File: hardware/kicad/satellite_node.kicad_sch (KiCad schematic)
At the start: 4 parts, among them U1 Seeed Studio XIAO ESP32S3, U2 SmartElex KX134-1211 (acceler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, U3 INMP441 (I2S microphone), U4 WS2812B x8 status ring

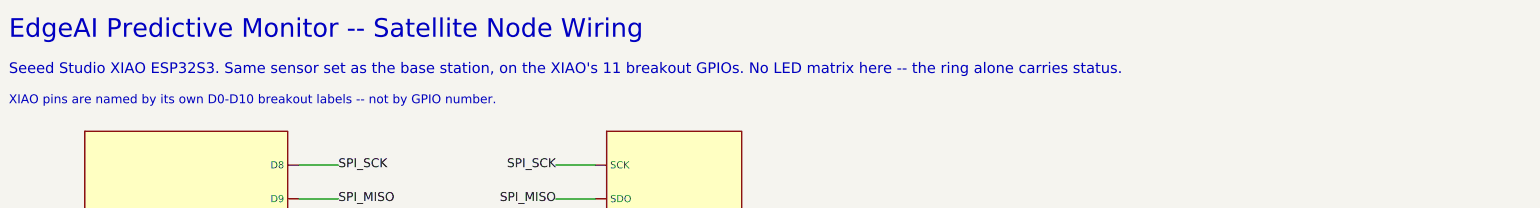
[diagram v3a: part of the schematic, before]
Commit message: schematics: shorten satellite-node subtitle to cut crop-driven whitespace
That subtitle line was the widest thing on the sheet -- 149 chars vs.
~83-134 on the other two diagrams -- so the auto-crop bounding box
stretched ~100mm past the actual circuit just to fit it, leaving a
dead strip on the right. Trimmed it to the same info in fewer words.

Co-Authored-By: Claude Sonnet 5 <noreply@anthropic.com>
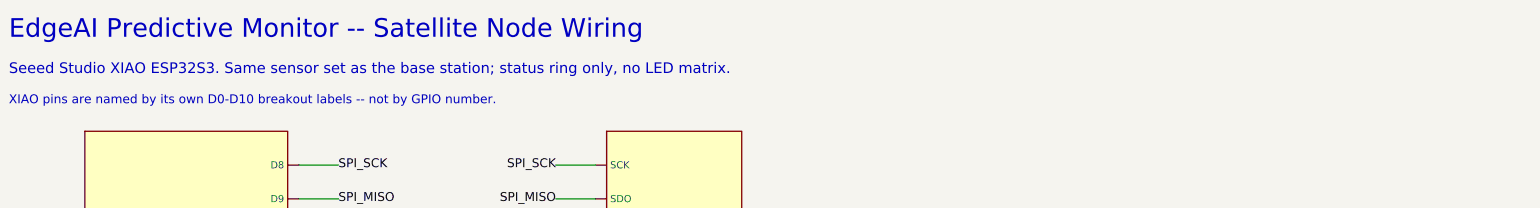
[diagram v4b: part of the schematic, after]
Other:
- note added: "Seeed Studio XIAO ESP32S3. Same sensor set as the base station; status ring only, no LED matrix."
- note removed: "Seeed Studio XIAO ESP32S3. Same sensor set as the base station, on the XIAO's 11 breakout GPIOs. No LED matrix here -- the ring alone carries status."
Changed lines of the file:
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@@
 		(effects (font (size 4.2 4.2)) (justify left))
 	)
-	(text "Seeed Studio XIAO ESP32S3. Same sensor set as the base station, on the XIAO's 11 breakout GPIOs. No LED matrix here -- the ring alone carries status."
+	(text "Seeed Studio XIAO ESP32S3. Same sensor set as the base station; status ring only, no LED matrix."
 		(exclude_from_sim no)
 		(at 20 34 0)
@@
 		(instances
 			(project "epm"
-				(path "/b0fb9a1d-4179-43c2-8546-24e0d59c6c4d"
+				(path "/f496122b-d5f3-4e05-9a34-a035c40fc367"
 					(reference "U1")
 					(unit 1)
@@
 		(on_board yes)
 		(dnp no)
-		(property "Reference" "#PWRb905"
+		(property "Reference" "#PWR1534"
 			(at 94.29 118.2 0)
 			(effects (font (size 1.27 1.27)) (hide yes))
@@
 		(instances
 			(project "epm"
-				(path "/b0fb9a1d-4179-43c2-8546-24e0d59c6c4d"
-					(reference "#PWRb905")
+				(path "/f496122b-d5f3-4e05-9a34-a035c40fc367"
+					(reference "#PWR1534")
 					(unit 1)
 				)
@@
 		(on_board yes)
 		(dnp no)
-		(property "Reference" "#PWR753b"
+		(property "Reference" "#PWR40eb"
 			(at 94.29 125.82 0)
 			(effects (font (size 1.27 1.27)) (hide yes))
@@
 		(instances
 			(project "epm"
-				(path "/b0fb9a1d-4179-43c2-8546-24e0d59c6c4d"
-					(reference "#PWR753b")
+				(path "/f496122b-d5f3-4e05-9a34-a035c40fc367"
+					(reference "#PWR40eb")
 					(unit 1)
 				)
@@
 		(on_board yes)
 		(dnp no)
-		(property "Reference" "#PWRd3a9"
+		(property "Reference" "#PWR83cc"
 			(at 94.29 133.44 0)
 			(effects (font (size 1.27 1.27)) (hide yes))
@@
 		(instances
 			(project "epm"
-				(path "/b0fb9a1d-4179-43c2-8546-24e0d59c6c4d"
-					(reference "#PWRd3a9")
+				(path "/f496122b-d5f3-4e05-9a34-a035c40fc367"
+					(reference "#PWR83cc")
 					(unit 1)
 				)
@@
 		(instances
 			(project "epm"
-				(path "/b0fb9a1d-4179-43c2-8546-24e0d59c6c4d"
+				(path "/f496122b-d5f3-4e05-9a34-a035c40fc367"
 					(reference "U2")
 					(unit 1)
@@
 		(on_board yes)
 		(dnp no)
-		(property "Reference" "#PWR9c86"
+		(property "Reference" "#PWR5d82"
 			(at 143.32999999999998 87.72 0)
 			(effects (font (size 1.27 1.27)) (hide yes))
@@
 		(instances
 			(project "epm"
-				(path "/b0fb9a1d-4179-43c2-8546-24e0d59c6c4d"
-					(reference "#PWR9c86")
+				(path "/f496122b-d5f3-4e05-9a34-a035c40fc367"
+					(reference "#PWR5d82")
 					(unit 1)
 				)
@@
 		(on_board yes)
 		(dnp no)
-		(property "Reference" "#PWRb8b9"
+		(property "Reference" "#PWR1843"
 			(at 143.32999999999998 95.34 0)
 			(effects (font (size 1.27 1.27)) (hide yes))
@@
 		(instances
 			(project "epm"
-				(path "/b0fb9a1d-4179-43c2-8546-24e0d59c6c4d"
-					(reference "#PWRb8b9")
+				(path "/f496122b-d5f3-4e05-9a34-a035c40fc367"
+					(reference "#PWR1843")
 					(unit 1)
 				)
@@
 		(instances
 			(project "epm"
-				(path "/b0fb9a1d-4179-43c2-8546-24e0d59c6c4d"
+				(path "/f496122b-d5f3-4e05-9a34-a035c40fc367"
 					(reference "U3")
 					(unit 1)
@@
 		(on_board yes)
 		(dnp no)
-		(property "Reference" "#PWR7f09"
+		(property "Reference" "#PWR40e0"
 			(at 144.60000000000002 147.20000000000002 0)
 			(effects (font (size 1.27 1.27)) (hide yes))
@@
 		(instances
 			(project "epm"
-				(path "/b0fb9a1d-4179-43c2-8546-24e0d59c6c4d"
-					(reference "#PWR7f09")
+				(path "/f496122b-d5f3-4e05-9a34-a035c40fc367"
+					(reference "#PWR40e0")
 					(unit 1)
 				)
@@
 		(on_board yes)
 		(dnp no)
-		(property "Reference" "#PWR97c5"
+		(property "Reference" "#PWR623f"
 			(at 144.60000000000002 154.82000000000002 0)
 			(effects (font (size 1.27 1.27)) (hide yes))
@@
 		(instances
 			(project "epm"
-				(path "/b0fb9a1d-4179-43c2-8546-24e0d59c6c4d"
-					(reference "#PWR97c5")
+				(path "/f496122b-d5f3-4e05-9a34-a035c40fc367"
+					(reference "#PWR623f")
 					(unit 1)
 				)
@@
 		(on_board yes)
 		(dnp no)
-		(property "Reference" "#PWR6390"
+		(property "Reference" "#PWRc5e7"
 			(at 144.60000000000002 162.44000000000003 0)
 			(effects (font (size 1.27 1.27)) (hide yes))
@@
 		(instances
 			(project "epm"
-				(path "/b0fb9a1d-4179-43c2-8546-24e0d59c6c4d"
-					(reference "#PWR6390")
+				(path "/f496122b-d5f3-4e05-9a34-a035c40fc367"
+					(reference "#PWRc5e7")
 					(unit 1)
 				)
@@
 		(instances
 			(project "epm"
-				(path "/b0fb9a1d-4179-43c2-8546-24e0d59c6c4d"
+				(path "/f496122b-d5f3-4e05-9a34-a035c40fc367"
 					(reference "U4")
 					(unit 1)
@@
 		(on_board yes)
 		(dnp no)
-		(property "Reference" "#PWR42ca"
+		(property "Reference" "#PWRbdb7"
 			(at 144.60000000000002 199.06 0)
 			(effects (font (size 1.27 1.27)) (hide yes))
@@
 		(instances
 			(project "epm"
-				(path "/b0fb9a1d-4179-43c2-8546-24e0d59c6c4d"
-					(reference "#PWR42ca")
+				(path "/f496122b-d5f3-4e05-9a34-a035c40fc367"
+					(reference "#PWRbdb7")
 					(unit 1)
 				)
@@
 		(on_board yes)
 		(dnp no)
-		(property "Reference" "#PWR17d9"
+		(property "Reference" "#PWRbfdd"
 			(at 144.60000000000002 206.68 0)
 			(effects (font (size 1.27 1.27)) (hide yes))
@@
 		(instances
 			(project "epm"
-				(path "/b0fb9a1d-4179-43c2-8546-24e0d59c6c4d"
-					(reference "#PWR17d9")
-					(unit 1)
-				)
+				(path "/f496122b-d5f3-4e05-9a34-a035c40fc367"
+					(reference "#PWRbfdd")
+					(unit 1)
+				)

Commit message: schematics: fix satellite pin map, rename accel nets, hi-res exports, KiCad projects
- satellite_node: ACC_CS/ACC_INT/MIC_WS/MIC_SD were wrong vs
  satellite/include/board_pins.h (used D3/D2/D0/D4; firmware drives
  D6/D7/D2/D3). Now transcribed straight from the header.
- base + satellite: SPI_SCK/MISO/MOSI nets renamed to ACC_SCK/ACC_MISO/
  ACC_MOSI so the accelerometer bus reads consistently with ACC_CS/ACC_INT.
- exports: SVG now --exclude-drawing-sheet; raster bumped to scale=5.0
  (~3.6-3.9k px) for headroom against Hackster's imgix auto=compress;
  report PNGs flattened to true PNG-24 (no alpha) + sibling JPEGs (q92).
  Crop simplified to a plain ink bbox.
- gen.py write_pro() now emits a real minimal .kicad_pro per board
  (sheets -> sch root UUID) so each opens as a self-contained project;
  make_bundles.py zips pro+sch+pdf into dist/ for Hackster Attachments
  (dist/ git-ignored).

Co-Authored-By: Claude Sonnet 5 <noreply@anthropic.com>
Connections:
- net SPI_MISO renamed ACC_MISO
- net SPI_MOSI renamed ACC_MOSI
- net SPI_SCK renamed ACC_SCK
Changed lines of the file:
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@@
 		(stroke (width 0) (type default))
 	)
-	(label "SPI_SCK"
+	(label "ACC_SCK"
 		(at 94.29 55.62 0)
 		(effects (font (size 2.0 2.0)) (justify left))
 	)
-	(label "SPI_MISO"
+	(label "ACC_MISO"
 		(at 94.29 63.24 0)
 		(effects (font (size 2.0 2.0)) (justify left))
 	)
-	(label "SPI_MOSI"
+	(label "ACC_MOSI"
 		(at 94.29 70.86 0)
 		(effects (font (size 2.0 2.0)) (justify left))
@@
 		(effects (font (size 2.0 2.0)) (justify left))
 	)
-	(label "SPI_SCK"
+	(label "ACC_SCK"
 		(at 143.32999999999998 55.620000000000005 0)
 		(effects (font (size 2.0 2.0)) (justify right))
 	)
-	(label "SPI_MISO"
+	(label "ACC_MISO"
 		(at 143.32999999999998 63.24 0)
 		(effects (font (size 2.0 2.0)) (justify right))
 	)
-	(label "SPI_MOSI"
+	(label "ACC_MOSI"
 		(at 143.32999999999998 70.86 0)
 		(effects (font (size 2.0 2.0)) (justify right))
@@
 		(instances
 			(project "epm"
-				(path "/f496122b-d5f3-4e05-9a34-a035c40fc367"
+				(path "/eb09b952-6273-4b00-b988-117cd571ae26"
 					(reference "U1")
 					(unit 1)
@@
 		(on_board yes)
 		(dnp no)
-		(property "Reference" "#PWR1534"
+		(property "Reference" "#PWRcdb7"
 			(at 94.29 118.2 0)
 			(effects (font (size 1.27 1.27)) (hide yes))
@@
 		(instances
 			(project "epm"
-				(path "/f496122b-d5f3-4e05-9a34-a035c40fc367"
-					(reference "#PWR1534")
+				(path "/eb09b952-6273-4b00-b988-117cd571ae26"
+					(reference "#PWRcdb7")
 					(unit 1)
 				)
@@
 		(on_board yes)
 		(dnp no)
-		(property "Reference" "#PWR40eb"
+		(property "Reference" "#PWRa4df"
 			(at 94.29 125.82 0)
 			(effects (font (size 1.27 1.27)) (hide yes))
@@
 		(instances
 			(project "epm"
-				(path "/f496122b-d5f3-4e05-9a34-a035c40fc367"
-					(reference "#PWR40eb")
+				(path "/eb09b952-6273-4b00-b988-117cd571ae26"
+					(reference "#PWRa4df")
 					(unit 1)
 				)
@@
 		(on_board yes)
 		(dnp no)
-		(property "Reference" "#PWR83cc"
+		(property "Reference" "#PWR21c1"
 			(at 94.29 133.44 0)
 			(effects (font (size 1.27 1.27)) (hide yes))
@@
 		(instances
 			(project "epm"
-				(path "/f496122b-d5f3-4e05-9a34-a035c40fc367"
-					(reference "#PWR83cc")
+				(path "/eb09b952-6273-4b00-b988-117cd571ae26"
+					(reference "#PWR21c1")
 					(unit 1)
 				)
@@
 		(instances
 			(project "epm"
-				(path "/f496122b-d5f3-4e05-9a34-a035c40fc367"
+				(path "/eb09b952-6273-4b00-b988-117cd571ae26"
 					(reference "U2")
 					(unit 1)
@@
 		(on_board yes)
 		(dnp no)
-		(property "Reference" "#PWR5d82"
+		(property "Reference" "#PWR1ca8"
 			(at 143.32999999999998 87.72 0)
 			(effects (font (size 1.27 1.27)) (hide yes))
@@
 		(instances
 			(project "epm"
-				(path "/f496122b-d5f3-4e05-9a34-a035c40fc367"
-					(reference "#PWR5d82")
+				(path "/eb09b952-6273-4b00-b988-117cd571ae26"
+					(reference "#PWR1ca8")
 					(unit 1)
 				)
@@
 		(on_board yes)
 		(dnp no)
-		(property "Reference" "#PWR1843"
+		(property "Reference" "#PWR89b0"
 			(at 143.32999999999998 95.34 0)
 			(effects (font (size 1.27 1.27)) (hide yes))
@@
 		(instances
 			(project "epm"
-				(path "/f496122b-d5f3-4e05-9a34-a035c40fc367"
-					(reference "#PWR1843")
+				(path "/eb09b952-6273-4b00-b988-117cd571ae26"
+					(reference "#PWR89b0")
 					(unit 1)
 				)
@@
 		(instances
 			(project "epm"
-				(path "/f496122b-d5f3-4e05-9a34-a035c40fc367"
+				(path "/eb09b952-6273-4b00-b988-117cd571ae26"
 					(reference "U3")
 					(unit 1)
@@
 		(on_board yes)
 		(dnp no)
-		(property "Reference" "#PWR40e0"
+		(property "Reference" "#PWRd981"
 			(at 144.60000000000002 147.20000000000002 0)
 			(effects (font (size 1.27 1.27)) (hide yes))
@@
 		(instances
 			(project "epm"
-				(path "/f496122b-d5f3-4e05-9a34-a035c40fc367"
-					(reference "#PWR40e0")
+				(path "/eb09b952-6273-4b00-b988-117cd571ae26"
+					(reference "#PWRd981")
 					(unit 1)
 				)
@@
 		(on_board yes)
 		(dnp no)
-		(property "Reference" "#PWR623f"
+		(property "Reference" "#PWR7200"
 			(at 144.60000000000002 154.82000000000002 0)
 			(effects (font (size 1.27 1.27)) (hide yes))
@@
 		(instances
 			(project "epm"
-				(path "/f496122b-d5f3-4e05-9a34-a035c40fc367"
-					(reference "#PWR623f")
+				(path "/eb09b952-6273-4b00-b988-117cd571ae26"
+					(reference "#PWR7200")
 					(unit 1)
 				)
@@
 		(on_board yes)
 		(dnp no)
-		(property "Reference" "#PWRc5e7"
+		(property "Reference" "#PWRebd1"
 			(at 144.60000000000002 162.44000000000003 0)
 			(effects (font (size 1.27 1.27)) (hide yes))
@@
 		(instances
 			(project "epm"
-				(path "/f496122b-d5f3-4e05-9a34-a035c40fc367"
-					(reference "#PWRc5e7")
+				(path "/eb09b952-6273-4b00-b988-117cd571ae26"
+					(reference "#PWRebd1")
 					(unit 1)
 				)
@@
 		(instances
 			(project "epm"
-				(path "/f496122b-d5f3-4e05-9a34-a035c40fc367"
+				(path "/eb09b952-6273-4b00-b988-117cd571ae26"
 					(reference "U4")
 					(unit 1)
@@
 		(on_board yes)
 		(dnp no)
-		(property "Reference" "#PWRbdb7"
+		(property "Reference" "#PWR1c4d"
 			(at 144.60000000000002 199.06 0)
 			(effects (font (size 1.27 1.27)) (hide yes))
@@
 		(instances
 			(project "epm"
-				(path "/f496122b-d5f3-4e05-9a34-a035c40fc367"
-					(reference "#PWRbdb7")
+				(path "/eb09b952-6273-4b00-b988-117cd571ae26"
+					(reference "#PWR1c4d")
 					(unit 1)
 				)
@@
 		(on_board yes)
 		(dnp no)
-		(property "Reference" "#PWRbfdd"
+		(property "Reference" "#PWR49e2"
 			(at 144.60000000000002 206.68 0)
 			(effects (font (size 1.27 1.27)) (hide yes))
@@
 		(instances
 			(project "epm"
-				(path "/f496122b-d5f3-4e05-9a34-a035c40fc367"
-					(reference "#PWRbfdd")
-					(unit 1)
-				)
+				(path "/eb09b952-6273-4b00-b988-117cd571ae26"
+					(reference "#PWR49e2")
+					(unit 1)
+				)
